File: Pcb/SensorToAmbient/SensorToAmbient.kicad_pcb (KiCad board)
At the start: 2 copper layers, 48.1 x 77.7 mm, 29 parts, among them J1 Conn_01x04, J2 Conn_01x04, J3 Conn_01x04, J4 Conn_01x04, J5 Conn_01x04, J6 Conn_01x04, J7 Conn_01x02, J8 Conn_01x06, J9 Conn_01x06, SW1 SW_Push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

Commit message: Correct resistor const on pcb
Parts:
- R4: value R -> 100K
- R5: value 47K -> 100K
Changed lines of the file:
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@@
       (effects (font (size 1 1) (thickness 0.15)))
     )
-    (fp_text value R (at 0 1.75) (layer F.Fab)
+    (fp_text value 100K (at 0 1.75) (layer F.Fab)
       (effects (font (size 1 1) (thickness 0.15)))
     )
@@
       (effects (font (size 1 1) (thickness 0.15)))
     )
-    (fp_text value 47K (at 0 1.75) (layer F.Fab)
+    (fp_text value 100K (at 0 1.75) (layer F.Fab)
       (effects (font (size 1 1) (thickness 0.15)))
     )

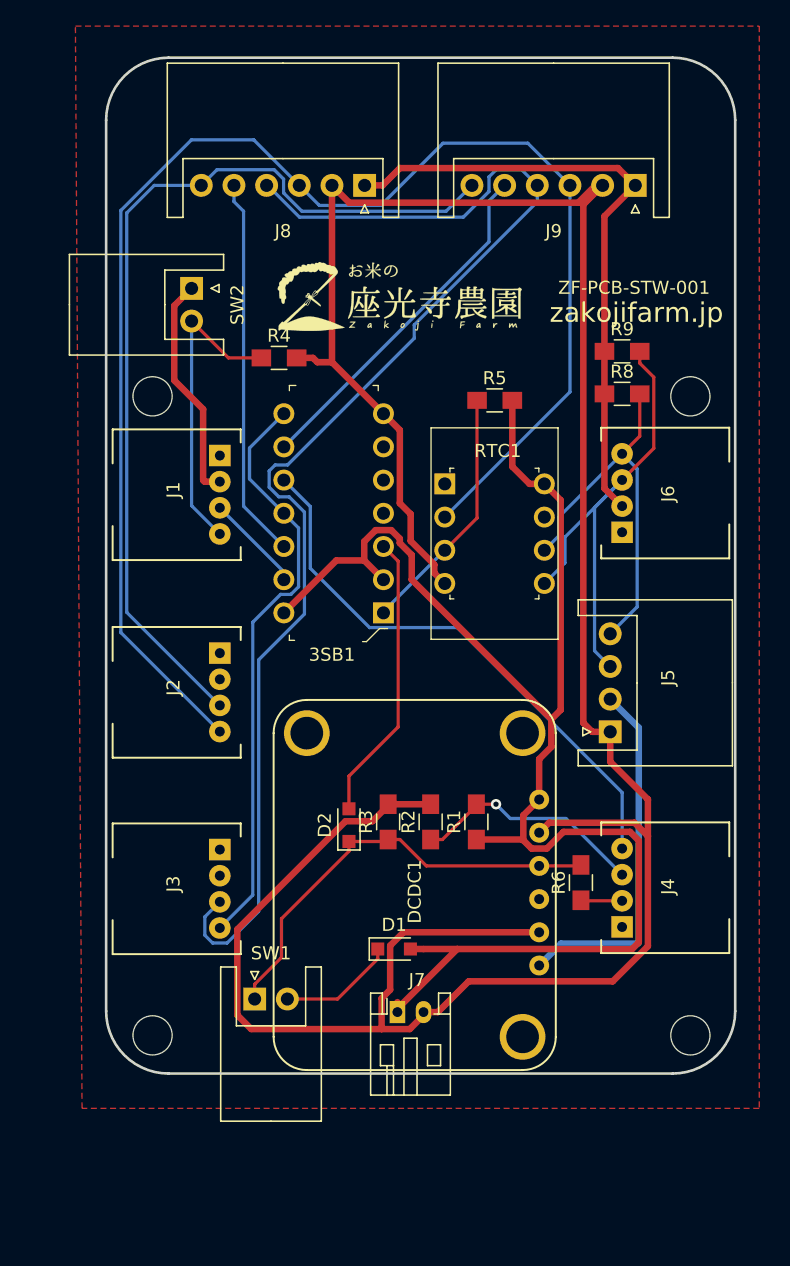
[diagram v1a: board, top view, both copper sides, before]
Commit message: Update silks on pcb for order
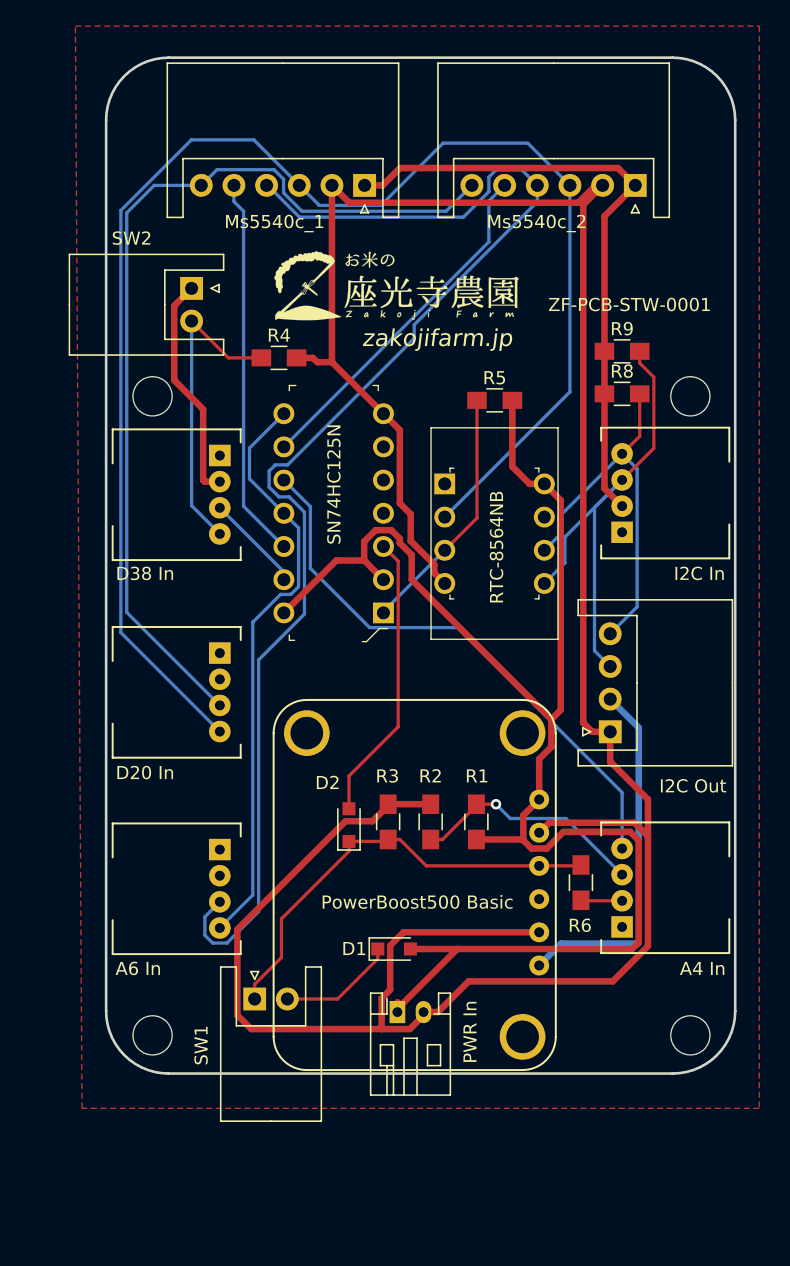
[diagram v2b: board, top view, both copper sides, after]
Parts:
- removed J2, J4: Conn_01x04, SensorToAmbient:Grove_2mm_4pin_angle2
- added A4 In: Conn_01x04, SensorToAmbient:Grove_2mm_4pin_angle2, F.Cu at (62.1, 76.3)
- added D20 In: Conn_01x04, SensorToAmbient:Grove_2mm_4pin_angle2, F.Cu at (31.4, 55.3)
- A6 In: renamed from J3
- D38 In: renamed from J1
- I2C In: renamed from J6
- I2C Out: renamed from J5
- PWR In: renamed from J7
- PowerBoost500 Basic: renamed from DCDC1
- moved G*** 0.86 mm to (45.2, 27.2)
- renumbered J8 to Ms5540c_1, J9 to Ms5540c_2, RTC1 to RTC-8564NB, 3SB1 to SN74HC125N
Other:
- board text added: "ZF-PCB-STW-0001"
- board text removed: "ZF-PCB-STW-001"

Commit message: Delete pullup resistors for I2C to replace with cpu internal pullups
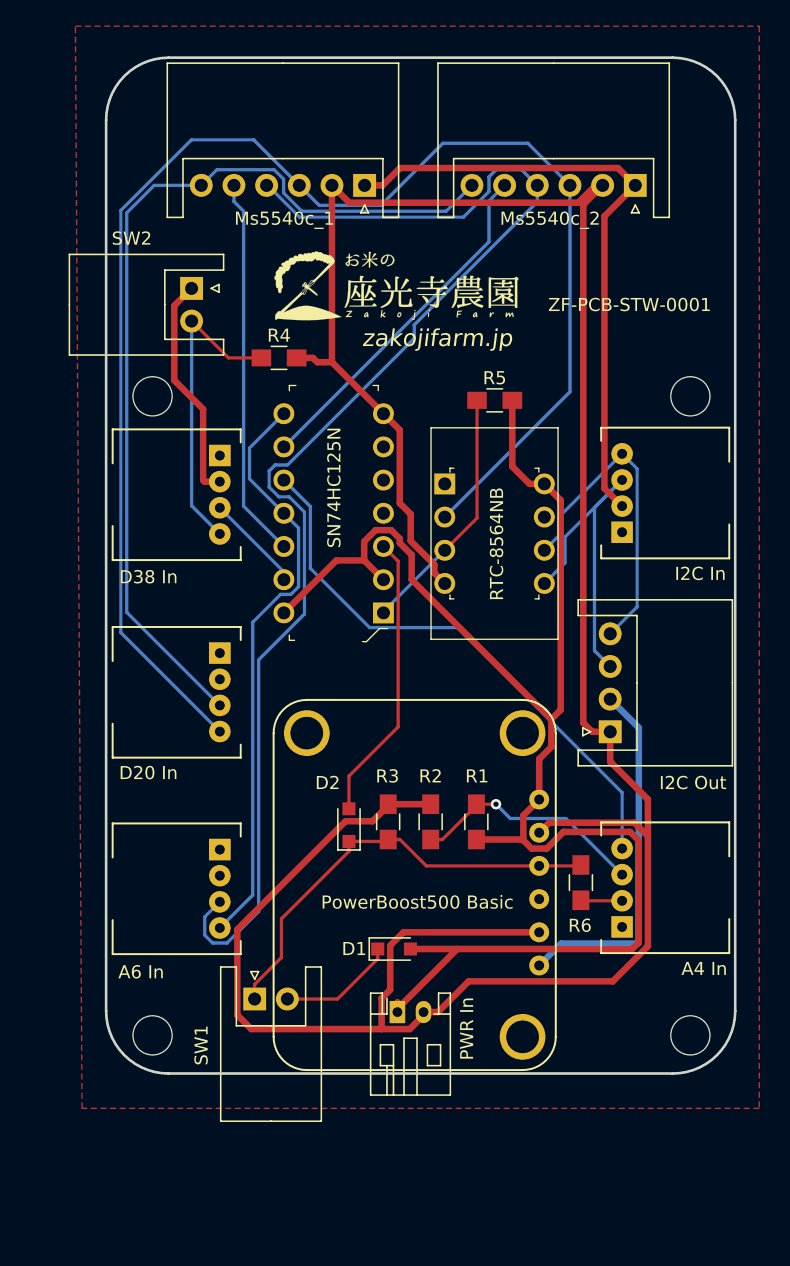
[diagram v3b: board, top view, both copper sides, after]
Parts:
- removed D20 In: Conn_01x04, SensorToAmbient:Grove_2mm_4pin_angle2
- removed R8, R9: 10K, Resistors_SMD:R_0805_HandSoldering
- added J2: D20 In, SensorToAmbient:Grove_2mm_4pin_angle2, F.Cu at (31.4, 55.3)
- DCDC1: renamed from PowerBoost500 Basic; value DCDC_PowerBoost500 -> PowerBoost500 Basic
- J1: renamed from D38 In; value Conn_01x04 -> D38 In
- J3: renamed from A6 In; value Conn_01x04 -> A6 In
- J4: renamed from A4 In; value Conn_01x04 -> A4 In
- J5: renamed from I2C Out; value Conn_01x04 -> I2C Out
- J6: renamed from I2C In; value Conn_01x04 -> I2C In
- J7: renamed from PWR In; value Conn_01x02 -> PWR In
- J8: renamed from Ms5540c_1; value Conn_01x06 -> Ms5540c_1
- J9: renamed from Ms5540c_2; value Conn_01x06 -> Ms5540c_2
- renumbered SN74HC125N to 3SB1, RTC-8564NB to RTC1
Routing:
- net Net-(J5-Pad3): track 37.7 -> 26.4 mm
- net Net-(J5-Pad4): track 30.1 -> 24.9 mm

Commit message: Move position of whole pcb
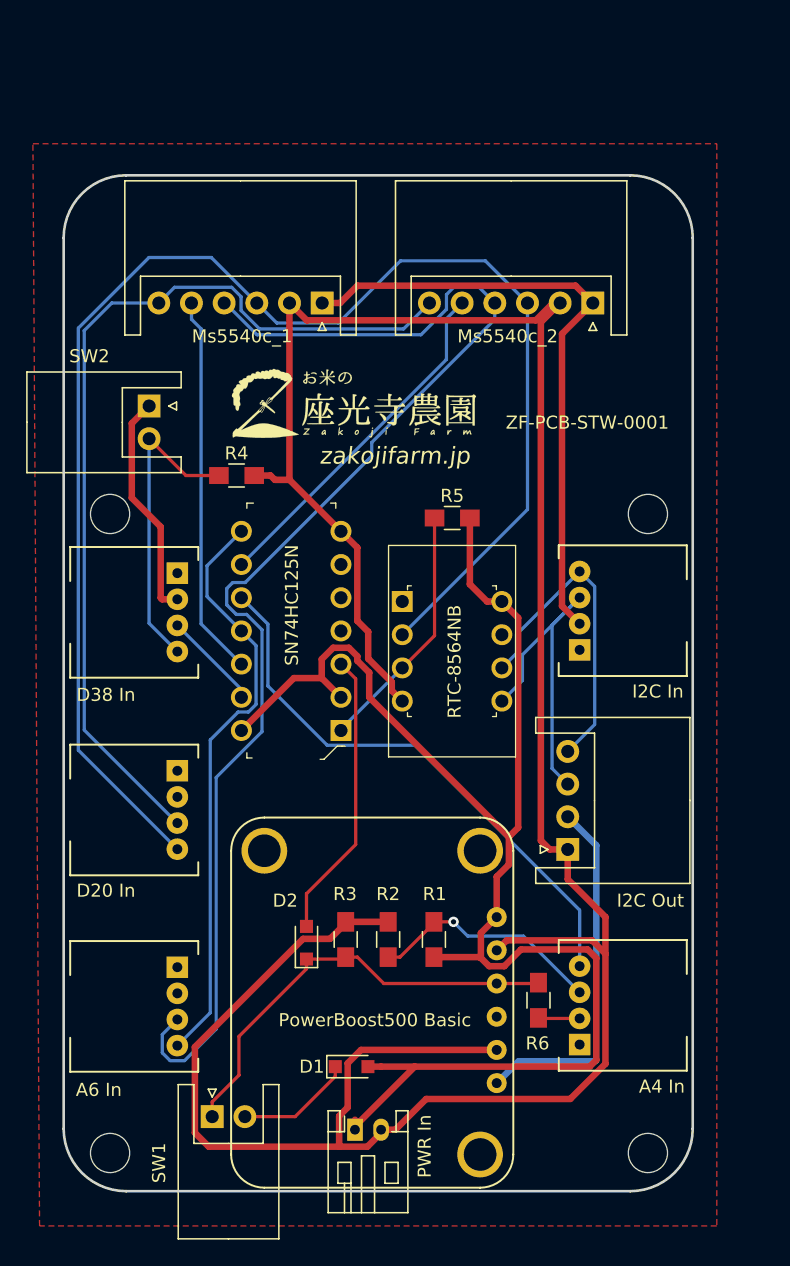
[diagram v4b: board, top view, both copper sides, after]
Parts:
- moved SW2 9.57 mm to (26.0, 36.4)
- moved 3SB1 9.57 mm to (40.6, 61.3)
- moved D1 9.57 mm to (41.5, 87.0)
- moved D2 9.57 mm to (38.0, 77.5)
- moved DCDC1 9.57 mm to (43.0, 82.1)
- moved J1 9.57 mm to (28.1, 49.2)
- moved J2 9.57 mm to (28.1, 64.3)
- moved J3 9.57 mm to (28.1, 79.4)
- moved J4 9.57 mm to (58.9, 85.3)
- moved J5 9.57 mm to (58.0, 70.4)
- moved J6 9.57 mm to (58.9, 55.1)
- moved J7 9.57 mm to (41.7, 91.8)
- moved J8 9.57 mm to (39.2, 28.6)
- moved J9 9.57 mm to (59.9, 28.6)
- moved R1 9.57 mm to (47.8, 77.2)
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
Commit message: Adjust pcb design for order
- Change a resistor for A4 power to diode
- Fit connectors on the inside of pcb edge
- Align wires
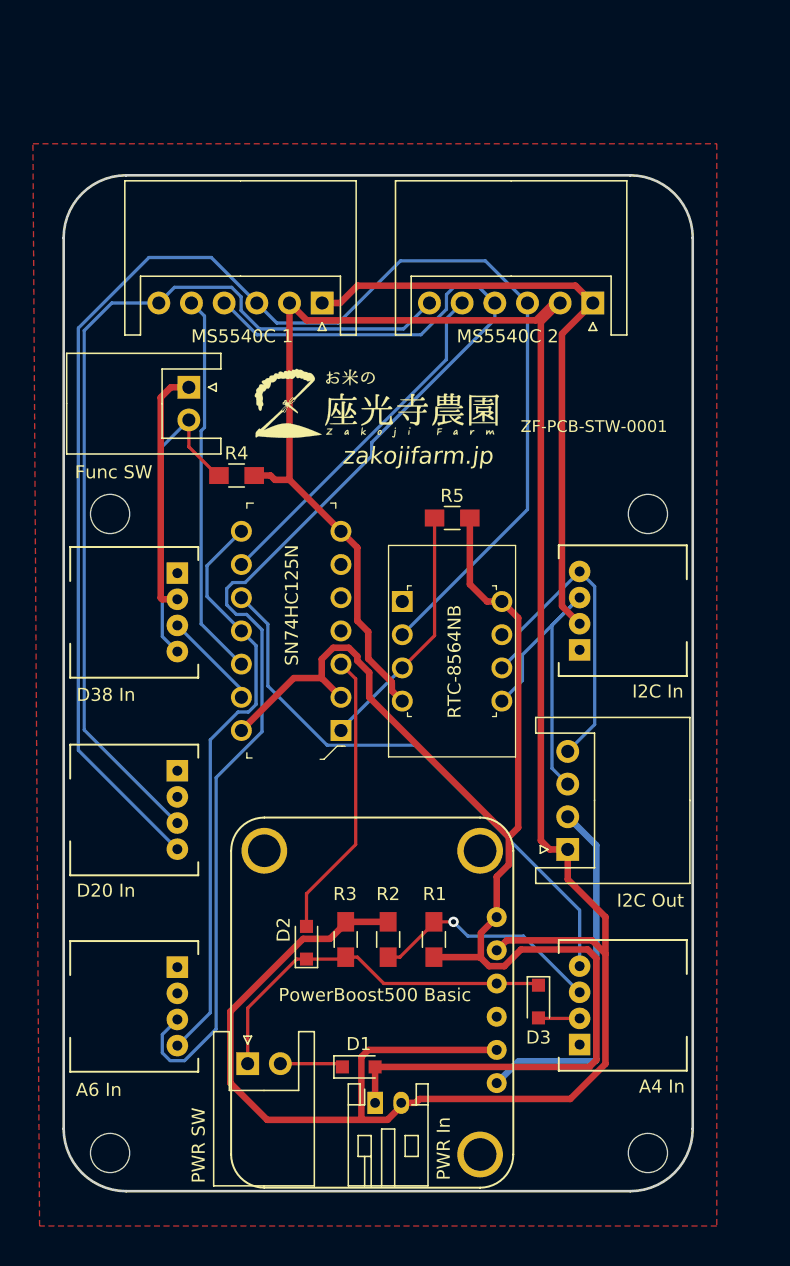
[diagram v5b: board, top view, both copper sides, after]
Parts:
- removed R6: 10K, Resistors_SMD:R_0805_HandSoldering
- removed REF**: MountingHole_3mm_rev, SensorToAmbient:MountingHole_3mm_rev
- added D3: D_Schottky, Diodes_SMD:D_SOD-323_HandSoldering, F.Cu at (55.8, 82.0)
- added REF4: MountingHole_3mm_rev, SensorToAmbient:MountingHole_3mm_rev, F.Cu at (64.1, 44.7)
- J8: value Ms5540c_1 -> MS5540C 1
- J9: value Ms5540c_2 -> MS5540C 2
- SW1: value SW_Push -> PWR SW
- SW2: value SW_Push -> Func SW
- moved SW1 4.88 mm to (33.5, 86.8)
- moved SW2 3.36 mm to (29.0, 35.0)
- moved J7 2.57 mm to (43.2, 89.8)
- moved G*** 1.75 mm to (43.7, 36.2)
- moved D1 0.55 mm to (42.0, 87.0)
- renumbered REF** to REF1, REF** to REF2, REF** to REF3
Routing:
- net GND: track 208.2 -> 197.2 mm
- net /PWR_BAT: track 117.1 -> 111.8 mm
- net Net-(D2-Pad1): track 33.7 -> 29.0 mm
- net Net-(D1-Pad1): track 9.00 -> 4.85 mm
- net /PWR3.3V_Switch: track 17.5 -> 19.1 mm
- net Net-(J1-Pad4): track 23.7 -> 24.3 mm

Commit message: Connect all GND pins of grove connectors to battery GND
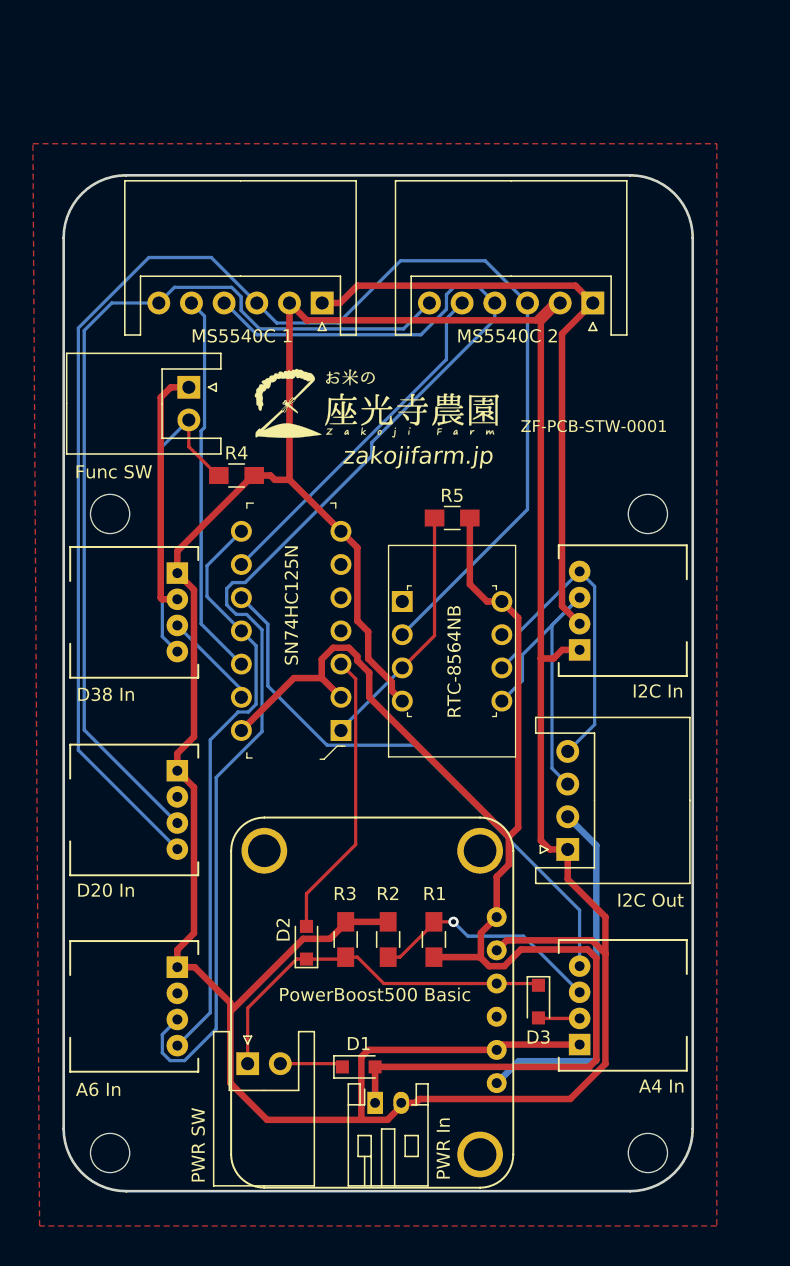
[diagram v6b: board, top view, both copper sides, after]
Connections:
- J1 pad 1: Net-(J1-Pad1) -> GND
- J2 pad 1: Net-(J2-Pad1) -> GND
- J3 pad 1: Net-(J3-Pad1) -> GND
- J4 pad 1: Net-(J4-Pad1) -> GND
- J6 pad 1: Net-(J6-Pad1) -> GND
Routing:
- net GND: track 197.2 -> 255.0 mm
